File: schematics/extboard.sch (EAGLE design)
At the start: 23 parts, among them U1 LTC1257, U2 LTC1257, X1-SD SDBMF, X2-JACK 1503_02

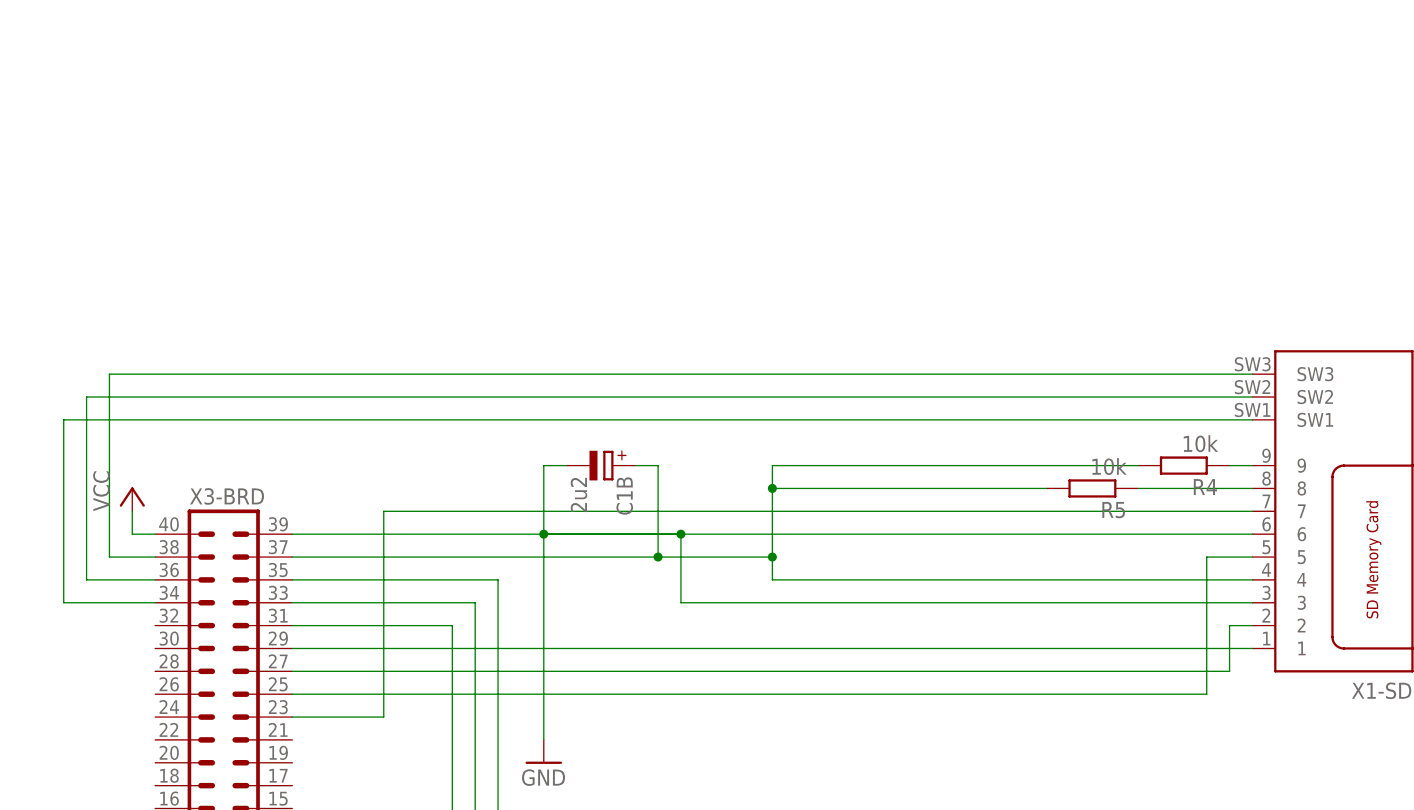
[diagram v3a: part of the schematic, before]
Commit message: schematic: Revision A iteration - jumpers for connecting DATA2 and DATA3 to board
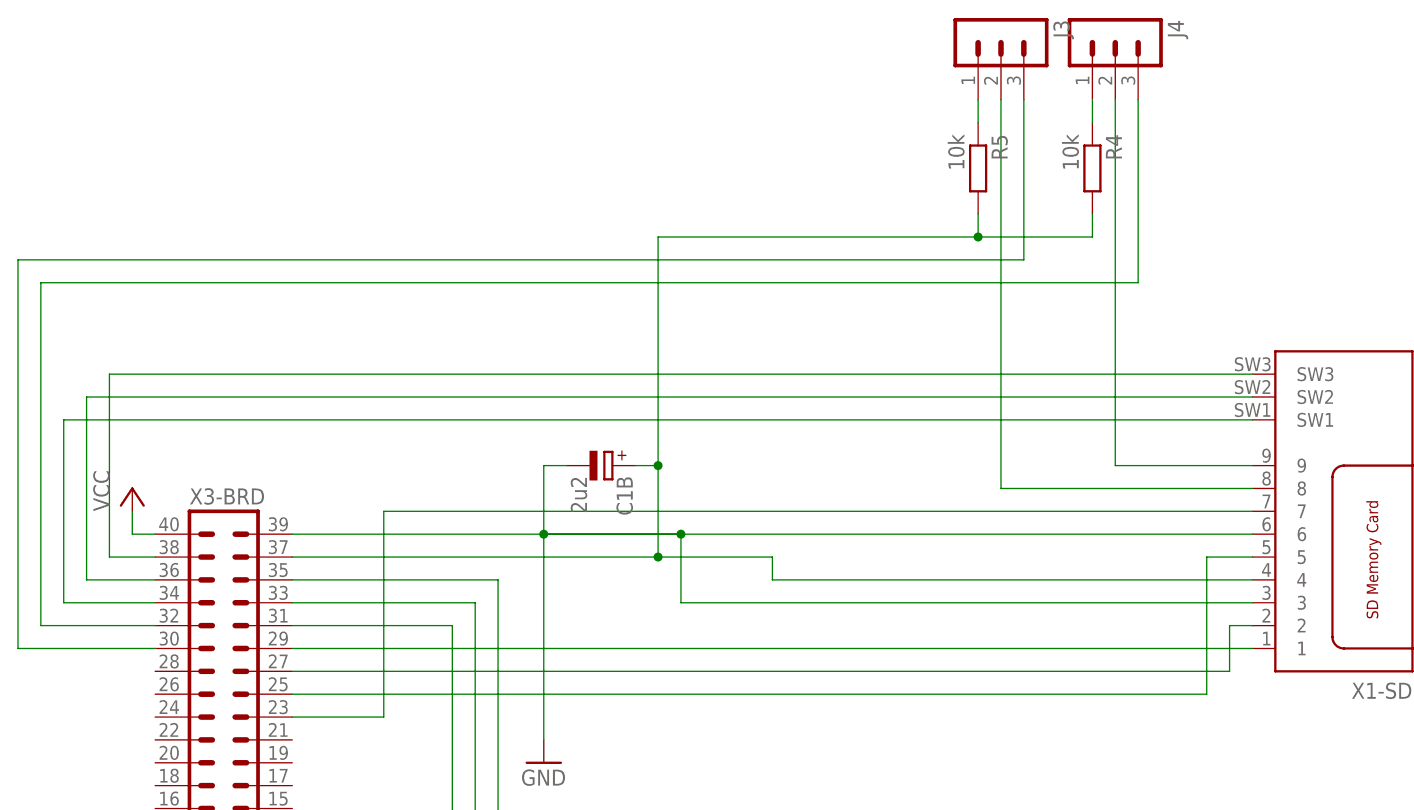
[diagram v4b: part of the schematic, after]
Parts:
- added J3, J4: (no value), con-lstb:MA03-1
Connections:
- removed net N$9 (its old number): R5.1, X1-SD.8
- new net N$27: J4.1, R4.1
- new net N$28: J3.2, X1-SD.8
- new net N$29: J4.2, X1-SD.9
- new net N$30: J4.3, X3-BRD.32
- new net N$31: J3.3, X3-BRD.30
- net N$10: now also J3.1, R5.1; no longer R4.1, X1-SD.9
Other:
- moved on the sheet: R4, R5
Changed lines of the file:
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@@
 <part name="X1-SD" library="farnell-sd" deviceset="SDBMF" device="" value=""/>
 <part name="C1B" library="rcl" deviceset="CPOL-EU" device="E2.5-7" value="2u2"/>
+<part name="J3" library="con-lstb" deviceset="MA03-1" device="">
+<attribute name="MF" value=""/>
+<attribute name="MPN" value=""/>
+<attribute name="OC_FARNELL" value="unknown"/>
+<attribute name="OC_NEWARK" value="unknown"/>
+</part>
+<part name="J4" library="con-lstb" deviceset="MA03-1" device="">
+<attribute name="MF" value=""/>
+<attribute name="MPN" value=""/>
+<attribute name="OC_FARNELL" value="unknown"/>
+<attribute name="OC_NEWARK" value="unknown"/>
+</part>
 </parts>
 <sheets>
@@
 <instance part="R1A" gate="G$1" x="73.66" y="17.78"/>
 <instance part="R2A" gate="G$1" x="104.14" y="7.62" rot="R90"/>
-<instance part="R4" gate="G$1" x="96.52" y="73.66" rot="R180"/>
-<instance part="R5" gate="G$1" x="86.36" y="71.12" rot="R180"/>
+<instance part="R4" gate="G$1" x="86.36" y="106.68" rot="R270"/>
+<instance part="R5" gate="G$1" x="73.66" y="106.68" rot="R270"/>
 <instance part="R3A" gate="G$1" x="12.7" y="22.86" rot="R90"/>
 <instance part="GND2" gate="1" x="63.5" y="7.62"/>
@@
 <instance part="X1-SD" gate="G$1" x="109.22" y="71.12" rot="R180"/>
 <instance part="C1B" gate="G$1" x="33.02" y="73.66" rot="R270"/>
+<instance part="J3" gate="G$1" x="76.2" y="121.92" rot="R270"/>
+<instance part="J4" gate="G$1" x="88.9" y="121.92" rot="R270"/>
 </instances>
 <busses>
@@
 </segment>
 </net>
+<net name="N$24" class="0">
+<segment>
+<pinref part="X1-SD" gate="G$1" pin="SW1"/>
+<wire x1="-27.94" y1="78.74" x2="104.14" y2="78.74" width="0.1524" layer="91"/>
+<pinref part="X3-BRD" gate="1" pin="34"/>
+<wire x1="-17.78" y1="58.42" x2="-27.94" y2="58.42" width="0.1524" layer="91"/>
+<wire x1="-27.94" y1="58.42" x2="-27.94" y2="78.74" width="0.1524" layer="91"/>
+</segment>
+</net>
+<net name="N$25" class="0">
+<segment>
+<pinref part="X1-SD" gate="G$1" pin="SW2"/>
+<wire x1="104.14" y1="81.28" x2="-25.4" y2="81.28" width="0.1524" layer="91"/>
+<wire x1="-25.4" y1="81.28" x2="-25.4" y2="60.96" width="0.1524" layer="91"/>
+<pinref part="X3-BRD" gate="1" pin="36"/>
+<wire x1="-25.4" y1="60.96" x2="-17.78" y2="60.96" width="0.1524" layer="91"/>
+</segment>
+</net>
+<net name="N$26" class="0">
+<segment>
+<pinref part="X1-SD" gate="G$1" pin="SW3"/>
+<wire x1="-22.86" y1="83.82" x2="104.14" y2="83.82" width="0.1524" layer="91"/>
+<wire x1="-22.86" y1="83.82" x2="-22.86" y2="63.5" width="0.1524" layer="91"/>
+<pinref part="X3-BRD" gate="1" pin="38"/>
+<wire x1="-22.86" y1="63.5" x2="-17.78" y2="63.5" width="0.1524" layer="91"/>
+</segment>
+</net>
 <net name="N$9" class="0">
 <segment>
-<pinref part="X1-SD" gate="G$1" pin="8"/>
-<pinref part="R5" gate="G$1" pin="1"/>
-<wire x1="104.14" y1="71.12" x2="91.44" y2="71.12" width="0.1524" layer="91"/>
-</segment>
-</net>
-<net name="N$10" class="0">
-<segment>
-<pinref part="X1-SD" gate="G$1" pin="9"/>
-<pinref part="R4" gate="G$1" pin="1"/>
-<wire x1="104.14" y1="73.66" x2="101.6" y2="73.66" width="0.1524" layer="91"/>
-</segment>
-</net>
-<net name="N$11" class="0">
-<segment>
+<pinref part="R4" gate="G$1" pin="2"/>
+<wire x1="86.36" y1="101.6" x2="86.36" y2="99.06" width="0.1524" layer="91"/>
 <pinref part="R5" gate="G$1" pin="2"/>
+<wire x1="86.36" y1="99.06" x2="73.66" y2="99.06" width="0.1524" layer="91"/>
+<wire x1="73.66" y1="99.06" x2="73.66" y2="101.6" width="0.1524" layer="91"/>
 <pinref part="C1B" gate="G$1" pin="+"/>
 <wire x1="38.1" y1="73.66" x2="35.56" y2="73.66" width="0.1524" layer="91"/>
@@
 <pinref part="X1-SD" gate="G$1" pin="4"/>
 <wire x1="104.14" y1="60.96" x2="50.8" y2="60.96" width="0.1524" layer="91"/>
-<wire x1="50.8" y1="63.5" x2="50.8" y2="71.12" width="0.1524" layer="91"/>
-<junction x="50.8" y="63.5"/>
-<wire x1="81.28" y1="71.12" x2="50.8" y2="71.12" width="0.1524" layer="91"/>
-<wire x1="50.8" y1="71.12" x2="50.8" y2="73.66" width="0.1524" layer="91"/>
-<junction x="50.8" y="71.12"/>
-<pinref part="R4" gate="G$1" pin="2"/>
-<wire x1="50.8" y1="73.66" x2="91.44" y2="73.66" width="0.1524" layer="91"/>
-</segment>
-</net>
-<net name="N$24" class="0">
-<segment>
-<pinref part="X1-SD" gate="G$1" pin="SW1"/>
-<wire x1="-27.94" y1="78.74" x2="104.14" y2="78.74" width="0.1524" layer="91"/>
-<pinref part="X3-BRD" gate="1" pin="34"/>
-<wire x1="-17.78" y1="58.42" x2="-27.94" y2="58.42" width="0.1524" layer="91"/>
-<wire x1="-27.94" y1="58.42" x2="-27.94" y2="78.74" width="0.1524" layer="91"/>
-</segment>
-</net>
-<net name="N$25" class="0">
-<segment>
-<pinref part="X1-SD" gate="G$1" pin="SW2"/>
-<wire x1="104.14" y1="81.28" x2="-25.4" y2="81.28" width="0.1524" layer="91"/>
-<wire x1="-25.4" y1="81.28" x2="-25.4" y2="60.96" width="0.1524" layer="91"/>
-<pinref part="X3-BRD" gate="1" pin="36"/>
-<wire x1="-25.4" y1="60.96" x2="-17.78" y2="60.96" width="0.1524" layer="91"/>
-</segment>
-</net>
-<net name="N$26" class="0">
-<segment>
-<pinref part="X1-SD" gate="G$1" pin="SW3"/>
-<wire x1="-22.86" y1="83.82" x2="104.14" y2="83.82" width="0.1524" layer="91"/>
-<wire x1="-22.86" y1="83.82" x2="-22.86" y2="63.5" width="0.1524" layer="91"/>
-<pinref part="X3-BRD" gate="1" pin="38"/>
-<wire x1="-22.86" y1="63.5" x2="-17.78" y2="63.5" width="0.1524" layer="91"/>
-</segment>
-</net>
+<wire x1="73.66" y1="99.06" x2="38.1" y2="99.06" width="0.1524" layer="91"/>
+<wire x1="38.1" y1="99.06" x2="38.1" y2="73.66" width="0.1524" layer="91"/>
+<junction x="73.66" y="99.06"/>
+<junction x="38.1" y="73.66"/>
+</segment>
+</net>
+<net name="N$10" class="0">
+<segment>
+<pinref part="R5" gate="G$1" pin="1"/>
+<pinref part="J3" gate="G$1" pin="1"/>
+<wire x1="73.66" y1="111.76" x2="73.66" y2="114.3" width="0.1524" layer="91"/>
+</segment>
+</net>
+<net name="N$27" class="0">
+<segment>
+<pinref part="R4" gate="G$1" pin="1"/>
+<pinref part="J4" gate="G$1" pin="1"/>
+<wire x1="86.36" y1="111.76" x2="86.36" y2="114.3" width="0.1524" layer="91"/>
+</segment>
+</net>
+<net name="N$28" class="0">
+<segment>
+<pinref part="J3" gate="G$1" pin="2"/>
+<wire x1="76.2" y1="114.3" x2="76.2" y2="71.12" width="0.1524" layer="91"/>
+<pinref part="X1-SD" gate="G$1" pin="8"/>
+<wire x1="76.2" y1="71.12" x2="104.14" y2="71.12" width="0.1524" layer="91"/>
+</segment>
+</net>
+<net name="N$29" class="0">
+<segment>
+<pinref part="X1-SD" gate="G$1" pin="9"/>
+<pinref part="J4" gate="G$1" pin="2"/>
+<wire x1="104.14" y1="73.66" x2="88.9" y2="73.66" width="0.1524" layer="91"/>
+<wire x1="88.9" y1="73.66" x2="88.9" y2="114.3" width="0.1524" layer="91"/>
+</segment>
+</net>
+<net name="N$30" class="0">
+<segment>
+<wire x1="91.44" y1="93.98" x2="-30.48" y2="93.98" width="0.1524" layer="91"/>
+<wire x1="-30.48" y1="93.98" x2="-30.48" y2="55.88" width="0.1524" layer="91"/>
+<pinref part="X3-BRD" gate="1" pin="32"/>
+<wire x1="-30.48" y1="55.88" x2="-17.78" y2="55.88" width="0.1524" layer="91"/>
+<pinref part="J4" gate="G$1" pin="3"/>
+<wire x1="91.44" y1="93.98" x2="91.44" y2="114.3" width="0.1524" layer="91"/>
+</segment>
+</net>
+<net name="N$31" class="0">
+<segment>
+<pinref part="X3-BRD" gate="1" pin="30"/>
+<wire x1="-17.78" y1="53.34" x2="-33.02" y2="53.34" width="0.1524" layer="91"/>
+<wire x1="-33.02" y1="53.34" x2="-33.02" y2="96.52" width="0.1524" layer="91"/>
+<wire x1="-33.02" y1="96.52" x2="78.74" y2="96.52" width="0.1524" layer="91"/>
+<pinref part="J3" gate="G$1" pin="3"/>
+<wire x1="78.74" y1="114.3" x2="78.74" y2="96.52" width="0.1524" layer="91"/>
+</segment>
+</net>

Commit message: schematics: Elevated to Revision B (2 prototypes in production)
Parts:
- C3A, C3B, C4A, C4B: device rcl:C-EU050-035X075 -> rcl:C-EU050-025X075
- X2-JACK: value 1503_02 -> 1503_07; device con-lumberg:1503_02 -> con-lumberg:1503_07; OC_FARNELL (none) -> unknown
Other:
- moved on the sheet: X2-JACK
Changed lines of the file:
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@@
 <part name="P+2" library="supply1" deviceset="VCC" device=""/>
 <part name="P+24" library="supply1" deviceset="VCC" device=""/>
-<part name="C3A" library="rcl" deviceset="C-EU" device="050-035X075" value="0u1"/>
-<part name="C4A" library="rcl" deviceset="C-EU" device="050-035X075" value="0u1"/>
+<part name="C3A" library="rcl" deviceset="C-EU" device="050-025X075" value="0u1"/>
+<part name="C4A" library="rcl" deviceset="C-EU" device="050-025X075" value="0u1"/>
 <part name="C1A" library="rcl" deviceset="CPOL-EU" device="E2.5-7" value="2u2"/>
 <part name="C2A" library="rcl" deviceset="CPOL-EU" device="E2.5-7" value="2u2"/>
@@
 <part name="GND8" library="supply1" deviceset="GND" device=""/>
 <part name="P+13" library="supply1" deviceset="VCC" device=""/>
-<part name="C3B" library="rcl" deviceset="C-EU" device="050-035X075" value="0u1"/>
-<part name="C4B" library="rcl" deviceset="C-EU" device="050-035X075" value="0u1"/>
+<part name="C3B" library="rcl" deviceset="C-EU" device="050-025X075" value="0u1"/>
+<part name="C4B" library="rcl" deviceset="C-EU" device="050-025X075" value="0u1"/>
 <part name="C2B" library="rcl" deviceset="CPOL-EU" device="E2.5-7" value="2u2"/>
 <part name="J1" library="con-lstb" deviceset="MA03-1" device=""/>
 <part name="J2" library="con-lstb" deviceset="MA03-1" device=""/>
-<part name="X2-JACK" library="con-lumberg" deviceset="1503_02" device=""/>
+<part name="X2-JACK" library="con-lumberg" deviceset="1503_?" device="07">
+<attribute name="OC_FARNELL" value="unknown"/>
+</part>
 <part name="X1-SD" library="farnell-sd" deviceset="SDBMF" device="" value=""/>
 <part name="C1B" library="rcl" deviceset="CPOL-EU" device="E2.5-7" value="2u2"/>
